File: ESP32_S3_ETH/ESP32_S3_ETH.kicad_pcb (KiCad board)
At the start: 4 copper layers, 100 x 58 mm, 86 parts, among them J1 USB_C_Receptacle_USB2.0_16P, J2 USB_C_Receptacle_USB2.0_16P, J3 J1B1211CCD, Q1 L8050QLT1G, Q2 L8050QLT1G, SW1 SW_Push, SW2 SW_Push, U1 ESP32-S3-WROOM-1-N8R2, U2 CP2102N-A02-GQFN28, U3 TC1264-3.3VDB, U4 W5500, Y1 ECS-2033-250-BN-TR3

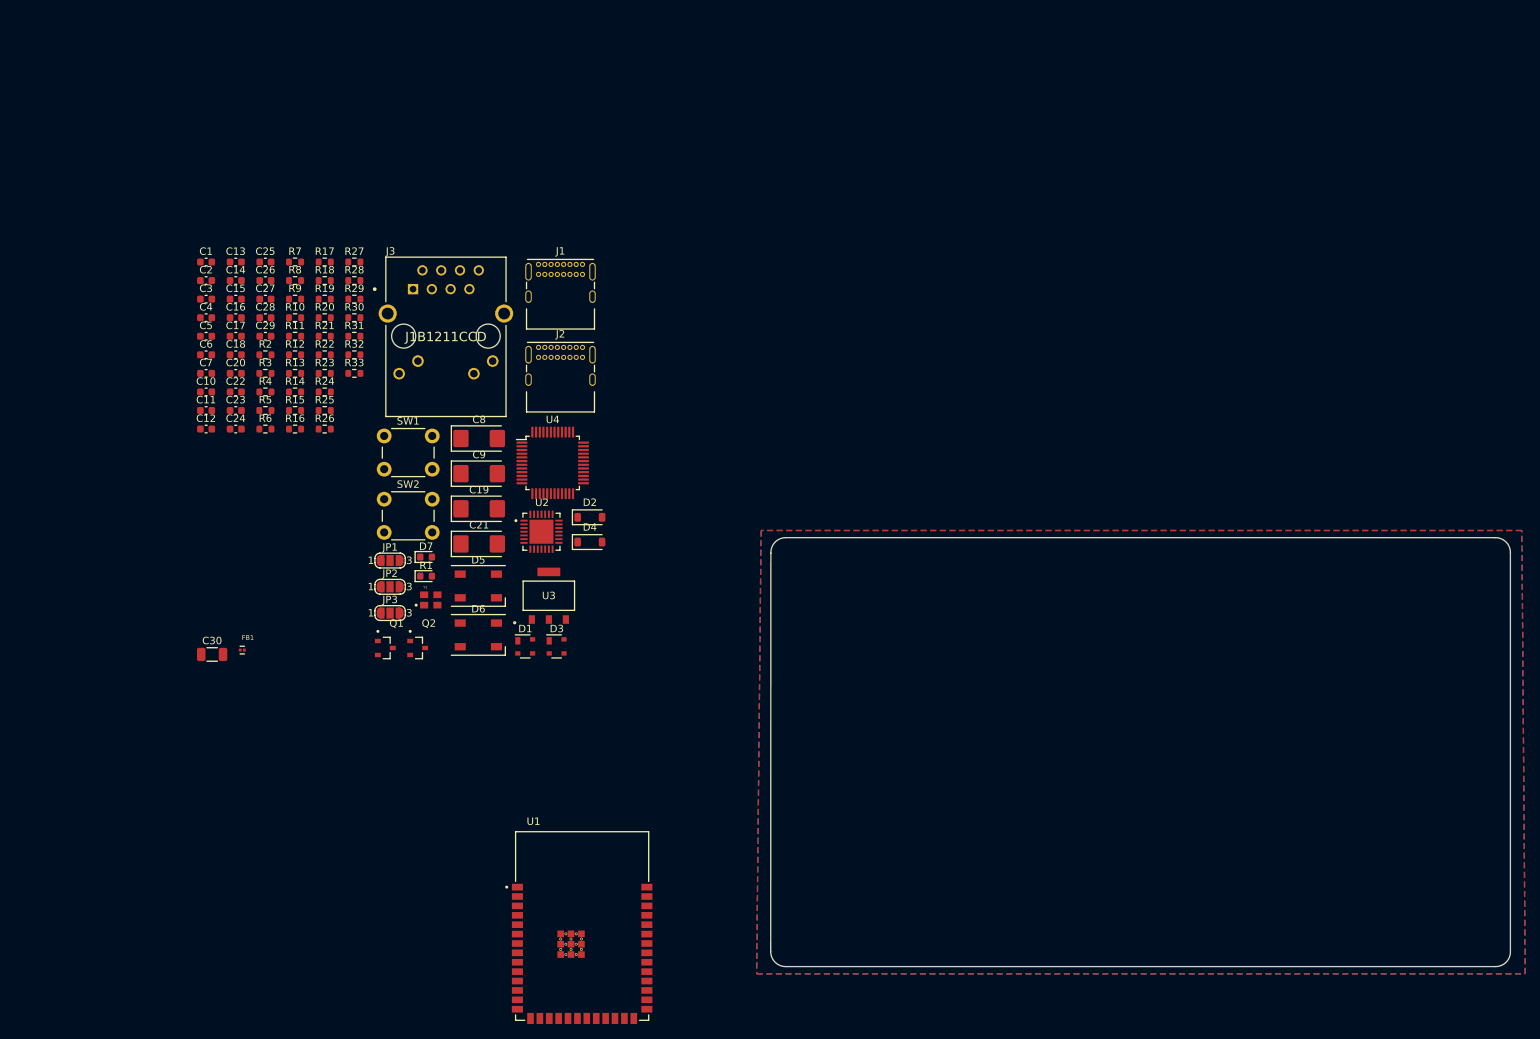
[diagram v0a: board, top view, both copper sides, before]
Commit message: ESP_ETH Schematic Finished, Routing Started on PCB
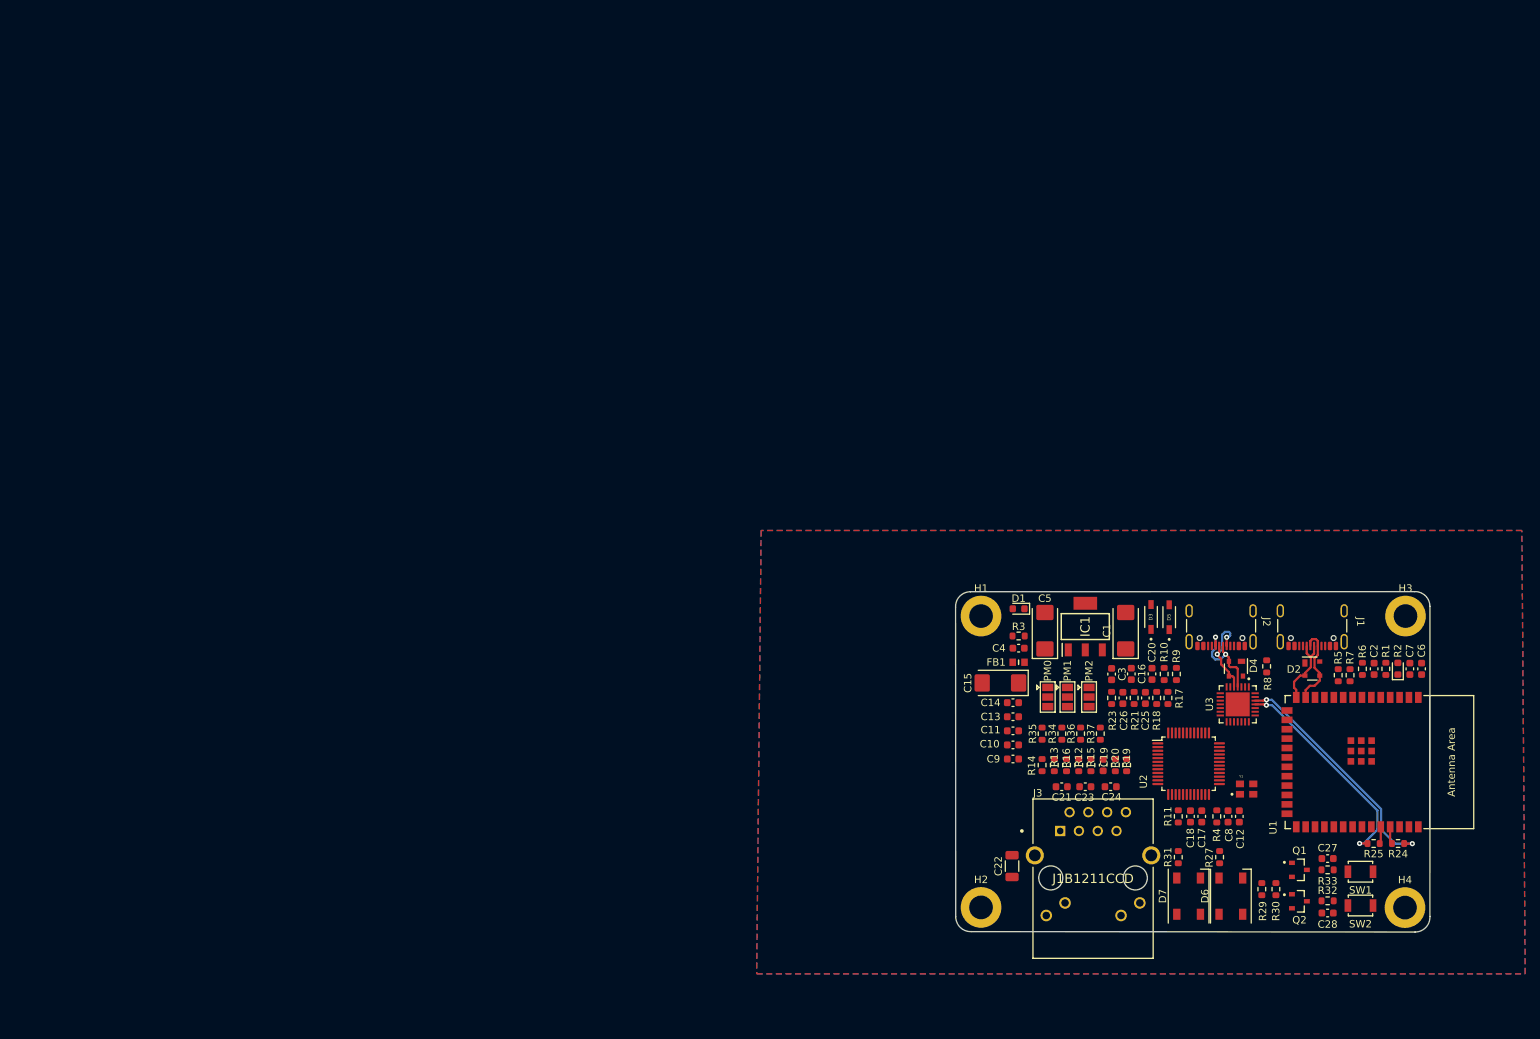
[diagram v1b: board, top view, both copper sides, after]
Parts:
- removed the C20 at (29.6, 46.8)
- removed the C21 at (62.5, 69.8)
- removed the C4 at (25.6, 39.2)
- removed JP1: PMODE2, Jumper:SolderJumper-3_P1.3mm_Open_RoundedPad1.0x1.5mm_NumberLabels
- removed JP2: PMODE1, Jumper:SolderJumper-3_P1.3mm_Open_RoundedPad1.0x1.5mm_NumberLabels
- removed JP3: PMODE0, Jumper:SolderJumper-3_P1.3mm_Open_RoundedPad1.0x1.5mm_NumberLabels
- removed the R2 at (33.6, 44.3)
- removed the R31 at (45.7, 41.8)
- removed the R32 at (45.7, 44.3)
- removed the R33 at (45.7, 46.8)
- removed the U3 at (72.0, 76.8)
- added C2: 1uF, Capacitor_SMD:C_0603_1608Metric, F.Cu at (183.6, 86.7)
- added H1: M3_1, MountingHole:MountingHole_3.2mm_M3_ISO14580_Pad, F.Cu at (130.4, 79.6)
- added H2: M3_3, MountingHole:MountingHole_3.2mm_M3_ISO14580_Pad, F.Cu at (130.4, 119.0)
- added H3: M3_2, MountingHole:MountingHole_3.2mm_M3_ISO14580_Pad, F.Cu at (187.8, 79.6)
- added H4: M3_4, MountingHole:MountingHole_3.2mm_M3_ISO14580_Pad, F.Cu at (187.7, 119.0)
- added IC1: TC1264-3.3VDB, KiCad:SOT230P700X180-4N, F.Cu at (144.5, 81.0)
- added PM0: 10K, Jumper:SolderJumper-3_P1.3mm_Open_Pad1.0x1.5mm, F.Cu at (139.4, 90.5)
- added PM1: 10K, Jumper:SolderJumper-3_P1.3mm_Open_Pad1.0x1.5mm, F.Cu at (142.1, 90.5)
- added PM2: 10K, Jumper:SolderJumper-3_P1.3mm_Open_Pad1.0x1.5mm, F.Cu at (145.0, 90.5)
- added R1: 10K, Resistor_SMD:R_0603_1608Metric, F.Cu at (185.2, 86.7)
- added R34: 0, Resistor_SMD:R_0603_1608Metric, F.Cu at (141.3, 95.5)
- added R35: 0, Resistor_SMD:R_0603_1608Metric, F.Cu at (138.7, 95.5)
- added R36: 0, Resistor_SMD:R_0603_1608Metric, F.Cu at (143.9, 95.5)
- added R37: 0, Resistor_SMD:R_0603_1608Metric, F.Cu at (146.5, 95.5)
- D3: renamed from D2; footprint Diode_SMD:D_SOD-123 -> 1N5819HW-7-F:SOD3715X145N
- D5: renamed from D4; footprint Diode_SMD:D_SOD-123 -> 1N5819HW-7-F:SOD3715X145N
- FB1: value BK0603LL121-T -> ~; footprint BK0603LL121-T:BEADC0603X33N -> fb:BEADC1608X95N
- J1, J2: footprint Connector_USB:USB_C_Receptacle_GCT_USB4085 -> Connector_USB:USB_C_Receptacle_GCT_USB4105-xx-A_16P_TopMnt_Horizontal
- R2: renamed from R1; value 47K -> 0
- SW1: renamed from SW2; value SW_Push -> RST; footprint Button_Switch_THT:SW_PUSH_6mm -> Button_Switch_SMD:SW_SPST_B3U-1000P
- SW2: renamed from SW1; value SW_Push -> BOOT; footprint Button_Switch_THT:SW_PUSH_6mm -> Button_Switch_SMD:SW_SPST_B3U-1000P
- U1: value ESP32-S3-WROOM-1-N8R2 -> ESP32-S3-WROOM-1; footprint ESP32-S3-WROOM-1-N8R2:XCVR_ESP32-S3-WROOM-1-N8R2 -> Espressif:ESP32-S3-WROOM-1
- moved C6 173.3 mm to (190.0, 86.7), turned to -90 degrees
- moved C7 171.0 mm to (188.4, 86.7), turned to -90 degrees
- moved C27 168.2 mm to (177.3, 112.4)
- moved C28 165.2 mm to (177.3, 119.8)
- moved R24 164.2 mm to (186.8, 110.4), turned to 180 degrees
- moved R25 160.1 mm to (183.5, 110.4)
- moved R32 159.5 mm to (177.3, 118.1), turned to 180 degrees
- moved R33 158.6 mm to (177.3, 113.9), turned to 180 degrees
- moved R6 153.0 mm to (182.0, 86.7), turned to -90 degrees
- moved R7 151.0 mm to (180.3, 87.6), turned to -90 degrees
- moved R5 150.7 mm to (178.7, 87.6), turned to 90 degrees
- moved R30 147.6 mm to (170.3, 116.5), turned to 90 degrees
- moved C12 147.3 mm to (165.3, 106.7), turned to -90 degrees
- moved SW2 146.5 mm to (181.7, 118.7), turned to 180 degrees
- moved C18 145.8 mm to (158.7, 106.7), turned to -90 degrees
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- renumbered C8 to C1, C15 to C10, C16 to C11, C22 to C12, C17 to C13, C18 to C14, C19 to C15, C3 to C16, C24 to C17, C25 to C18, C29 to C19, C5 to C20, C26 to C21, C30 to C22, C28 to C23, C27 to C24, C7 to C25, C6 to C26, C13 to C27, C12 to C28, C10 to C3, C11 to C4, C9 to C5, C1 to C6, C2 to C7, C23 to C8, C14 to C9, D7 to D1, D1 to D2, D3 to D4, D5 to D6, D6 to D7, R8 to R10, R22 to R11, R26 to R12, R23 to R13, R24 to R14, R27 to R15, R25 to R16, R13 to R17, R14 to R18, R29 to R19, R30 to R20, R10 to R21, R9 to R23, R11 to R24, R12 to R25, R19 to R27, R16 to R29, R21 to R3, R15 to R30, R20 to R31, R18 to R32, R17 to R33, R28 to R4, R3 to R5, R4 to R6, R5 to R7, R6 to R8, R7 to R9, U4 to U2, U2 to U3
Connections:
- net /GPIO19 renamed /GPIO_USB-
- net /GPIO20 renamed /GPIO_USB+
- net CHIP_PU renamed /CHIP_PU
- net ESP_3V3 renamed /ESP_3V3
- net GND1 renamed /CH_GND
- net VCC_3V3 renamed /VCC_3V3
- C1 pad 1: VCC_5V -> /VCC_5V
- C16 pad 1: VCC_5V -> /VCC_5V
- C20 pad 1: VCC_5V -> /VCC_5V
- C23 pad 1: Net-(U4-RXP) -> Net-(C23-Pad1)
- C24 pad 1: Net-(U4-RXN) -> Net-(C24-Pad1)
- C3 pad 1: VCC_5V -> /VCC_5V
- D2 pad 4: V_BUS -> /V_BUS
- D4 pad 4: V_BUS -> /V_BUS
- J1 pad A4: V_BUS -> /V_BUS
- J1 pad A9: V_BUS -> /V_BUS
- J1 pad B4: V_BUS -> /V_BUS
- J1 pad B9: V_BUS -> /V_BUS
- J2 pad A4: V_BUS -> /V_BUS
- J2 pad A9: V_BUS -> /V_BUS
- J2 pad B4: V_BUS -> /V_BUS
- J2 pad B9: V_BUS -> /V_BUS
- J3 pad 1: Net-(U4-TXP) -> Net-(J3-Pad1)
- J3 pad 3: Net-(U4-TXN) -> Net-(J3-Pad3)
- R12 pad 1: Net-(U4-RXP) -> Net-(C23-Pad1)
- R13 pad 2: Net-(U4-TXN) -> Net-(J3-Pad3)
- R14 pad 2: Net-(U4-TXP) -> Net-(J3-Pad1)
- R15 pad 1: Net-(U4-RXN) -> Net-(C24-Pad1)
- R17 pad 1: V_BUS -> /V_BUS
- R31 pad 1: /GPIO47 -> /GPIO1
- U1 pad 10: /GPIO17 -> unconnected-(U1-GPIO17/U1TXD/ADC2_CH6-Pad10)
- U1 pad 11: /GPIO18 -> unconnected-(U1-GPIO18/U1RXD/ADC2_CH7/CLK_OUT3-Pad11)
- U1 pad 12: /INTn -> /RSTn
- U1 pad 15: /GPIO3 -> unconnected-(U1-GPIO3/TOUCH3/ADC1_CH2-Pad15)
- U1 pad 16: /GPIO46 -> unconnected-(U1-GPIO46-Pad16)
- U1 pad 17: /MISO -> /INTn
- U1 pad 18: /SCSn -> /MOSI
- U1 pad 19: /SCLK -> /MISO
- U1 pad 20: /MOSI -> /SCLK
- U1 pad 21: /RSTn -> /SCSn
- U1 pad 22: /GPIO14 -> unconnected-(U1-GPIO14/TOUCH14/ADC2_CH3/FSPIWP/FSPIDQS/SUBSPIWP-Pad22)
- U1 pad 23: /GPIO21 -> unconnected-(U1-GPIO21-Pad23)
- U1 pad 24: /GPIO47 -> unconnected-(U1-GPIO47/SPICLK_P/SUBSPICLK_P_DIFF-Pad24)
- U1 pad 25: /GPIO48 -> unconnected-(U1-GPIO48/SPICLK_N/SUBSPICLK_N_DIFF-Pad25)
- U1 pad 26: /GPIO45 -> unconnected-(U1-GPIO45-Pad26)
- U1 pad 28: /GPIO35 -> unconnected-(U1-SPIIO6/GPIO35/FSPID/SUBSPID-Pad28)
- U1 pad 29: /GPIO36 -> unconnected-(U1-SPIIO7/GPIO36/FSPICLK/SUBSPICLK-Pad29)
- U1 pad 30: /GPIO37 -> unconnected-(U1-SPIDQS/GPIO37/FSPIQ/SUBSPIQ-Pad30)
- U1 pad 32: /GPIO39 -> unconnected-(U1-MTCK/GPIO39/CLK_OUT3/SUBSPICS1-Pad32)
- U1 pad 33: /GPIO40 -> unconnected-(U1-MTDO/GPIO40/CLK_OUT2-Pad33)
- U1 pad 34: /GPIO41 -> unconnected-(U1-MTDI/GPIO41/CLK_OUT1-Pad34)
- U1 pad 35: /GPIO42 -> unconnected-(U1-MTMS/GPIO42-Pad35)
- U1 pad 36: /ESP_U0_RXD0 -> /ESP_U0_TXD0
- U1 pad 37: /ESP_U0_TXD0 -> /ESP_U0_RXD0
- U1 pad 38: /GPIO2 -> unconnected-(U1-GPIO2/TOUCH2/ADC1_CH1-Pad38)
- U1 pad 4: /GPIO4 -> unconnected-(U1-GPIO4/TOUCH4/ADC1_CH3-Pad4)
- U1 pad 5: /GPIO5 -> unconnected-(U1-GPIO5/TOUCH5/ADC1_CH4-Pad5)
- U1 pad 6: /GPIO6 -> unconnected-(U1-GPIO6/TOUCH6/ADC1_CH5-Pad6)
- U1 pad 7: /GPIO7 -> unconnected-(U1-GPIO7/TOUCH7/ADC1_CH6-Pad7)
- U1 pad 8: /GPIO15 -> unconnected-(U1-GPIO15/U0RTS/ADC2_CH4/XTAL_32K_P-Pad8)
- U1 pad 9: /GPIO16 -> unconnected-(U1-GPIO16/U0CTS/ADC2_CH5/XTAL_32K_N-Pad9)
- U2 pad 1: Net-(U4-TXN) -> /TX_N
- U2 pad 2: Net-(U4-TXP) -> /TX_P
- U2 pad 5: Net-(U4-RXN) -> /RX_N
- U2 pad 6: Net-(U4-RXP) -> /RX_P
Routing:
- net Net-(U3-TXD): track 0.00 -> 32.1 mm, vias 0 -> 2
- net Net-(U3-RXD): track 0.00 -> 29.3 mm, vias 0 -> 2
- net /USB_D-: track 0.00 -> 13.7 mm, vias 0 -> 2
- net /USB_D+: track 0.00 -> 13.6 mm, vias 0 -> 2
- net /GPIO_USB-: track 0.00 -> 11.2 mm
- net /GPIO_USB+: track 0.00 -> 10.4 mm
- net /ESP_U0_RXD0: track 0.00 -> 2.36 mm
- net /ESP_U0_TXD0: track 0.00 -> 2.32 mm
- added copper zone on In2.Cu, net /VCC_3V3
- added copper zone on In1.Cu, net GND
- removed copper zone on In2.Cu, net GND
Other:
- board size 100 x 58 mm -> 64.1 x 46 mm

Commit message: Initial commit of the routing for the ethernet PCB for review and correction.
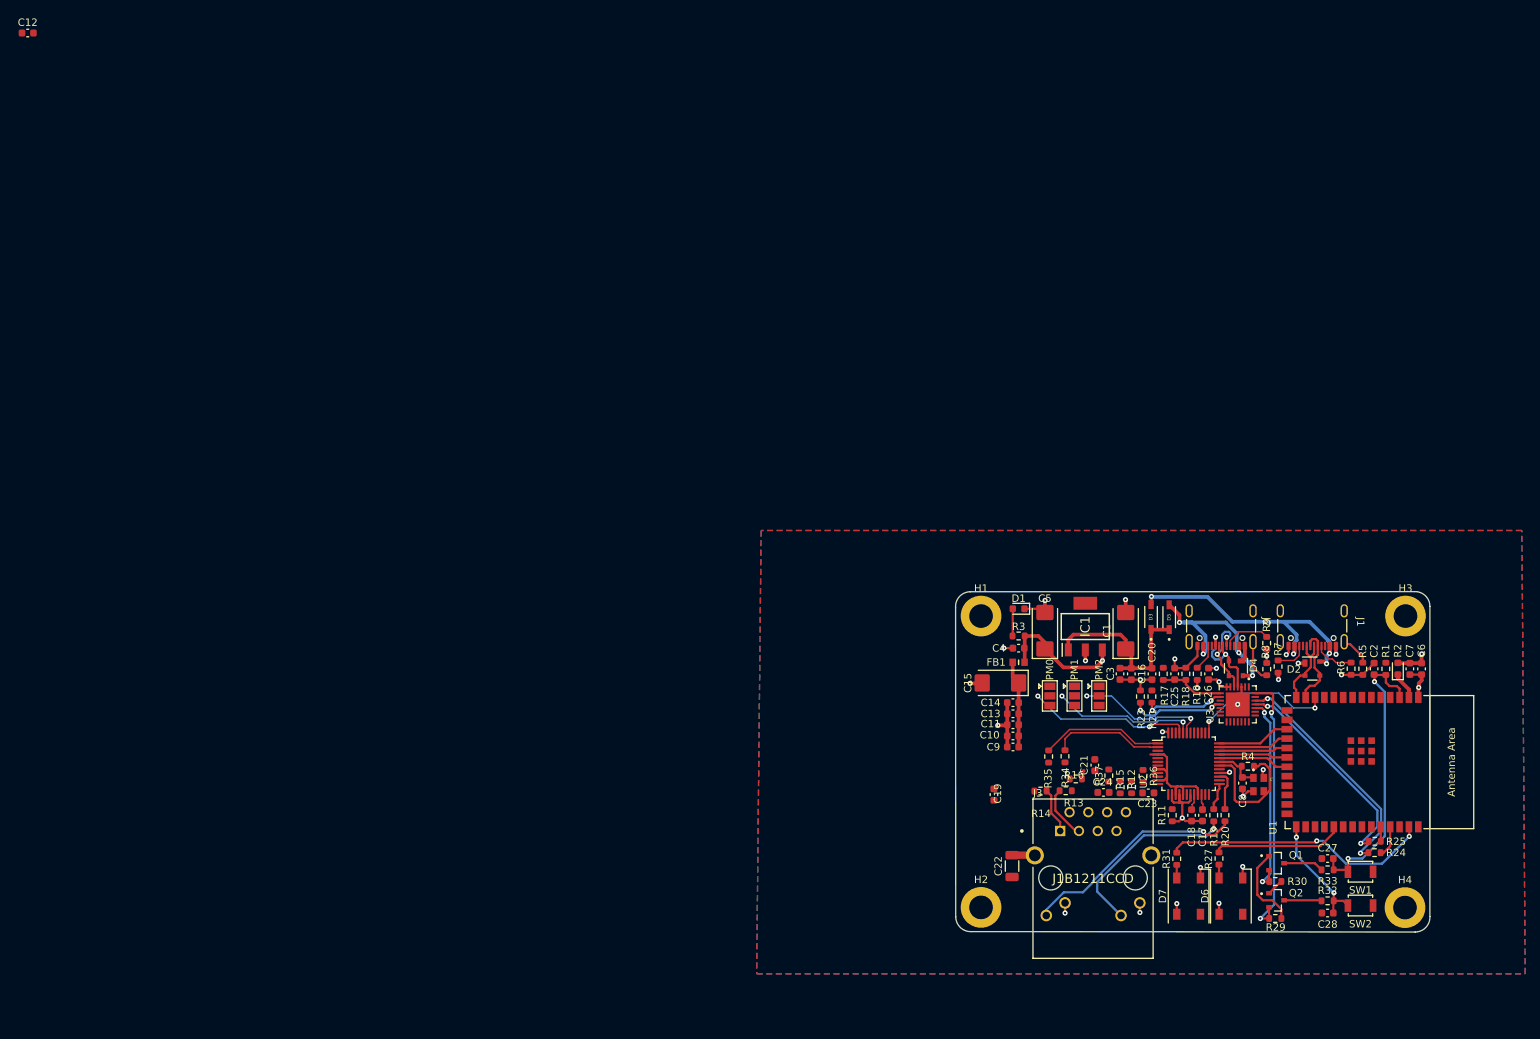
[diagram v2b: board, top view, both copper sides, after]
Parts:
- moved C12 195.1 mm to (1.50, 0.76), turned to 0 degrees
- moved R20 16.3 mm to (163.4, 106.5)
- moved C19 15.3 mm to (132.2, 103.7)
- moved R19 13.6 mm to (161.9, 106.5)
- moved R9 12.9 mm to (169.0, 83.2)
- moved C26 12.0 mm to (161.2, 87.4), turned to -90 degrees
- moved R36 10.2 mm to (152.3, 101.2)
- moved R7 9.80 mm to (170.6, 86.4)
- moved C23 8.56 mm to (153.0, 103.5)
- moved R4 7.98 mm to (166.5, 99.9), turned to 0 degrees
- moved R12 7.74 mm to (150.8, 102.7)
- moved R37 5.79 mm to (147.7, 101.2)
- moved C21 5.34 mm to (145.8, 99.8), turned to 90 degrees
- moved C25 5.13 mm to (156.6, 87.4)
- moved R18 5.12 mm to (158.1, 87.4)
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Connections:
- net Net-(C19-Pad1) renamed /RJ_RX_N
- net Net-(C23-Pad2) renamed /RJ_RX_P
- net Net-(J3-Pad1) renamed /RJ_TX_P
- net Net-(J3-Pad3) renamed /RJ_TX_N
- D2 pad 4: /V_BUS -> /V_BUS_JTAG
- D3 pad A: /V_BUS -> /V_BUS_JTAG
- J1 pad A4: /V_BUS -> /V_BUS_JTAG
- J1 pad A9: /V_BUS -> /V_BUS_JTAG
- J1 pad B4: /V_BUS -> /V_BUS_JTAG
- J1 pad B9: /V_BUS -> /V_BUS_JTAG
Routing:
- net GND: track 0.00 -> 73.3 mm, vias 0 -> 23
- net /CHIP_PU: track 0.00 -> 40.0 mm, vias 0 -> 2
- net /V_BUS_JTAG: track 0.00 -> 39.7 mm, vias 0 -> 4
- net /GPIO1: track 0.00 -> 36.5 mm, vias 0 -> 2
- net /DTR: track 0.00 -> 36.5 mm, vias 0 -> 2
- net /VCC_3V3: track 0.00 -> 34.4 mm, vias 0 -> 9
- net Net-(J3-CATHODE_GREEN): track 0.00 -> 30.7 mm, vias 0 -> 1
- net /A3V3: track 0.00 -> 28.7 mm
- net /RTS: track 0.00 -> 27.7 mm, vias 0 -> 2
- net /V_BUS: track 0.00 -> 27.4 mm, vias 0 -> 4
- net /VCC_5V: track 0.00 -> 26.0 mm
- net Net-(J3-CATHODE_YELLOW): track 0.00 -> 25.8 mm, vias 0 -> 1
- net /PMODE0: track 0.00 -> 22.0 mm, vias 0 -> 2
- net /RSTn: track 0.00 -> 19.7 mm, vias 0 -> 2
- net /PMODE1: track 0.00 -> 19.6 mm, vias 0 -> 2
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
